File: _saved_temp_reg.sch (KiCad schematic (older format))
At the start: 133 parts, among them IC1 ATMEGA644-P, P1 CONN_01X02, P10 CONN_01X04, P11 CONN_01X06, P12 CONN_01X02, P13 CONN_01X02, P15 CONN_01X02, P2 CONN_01X03, P3 CONN_01X03, P4 CONN_2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

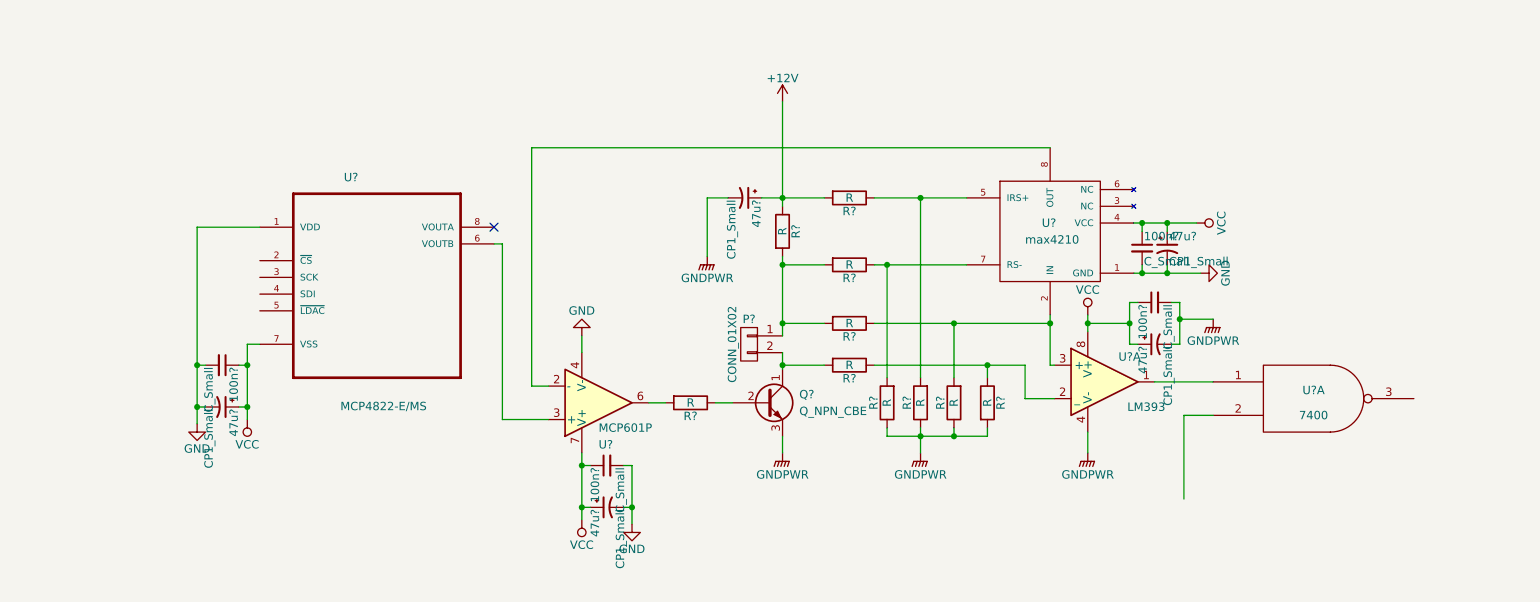
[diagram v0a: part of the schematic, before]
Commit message: change to power opamp
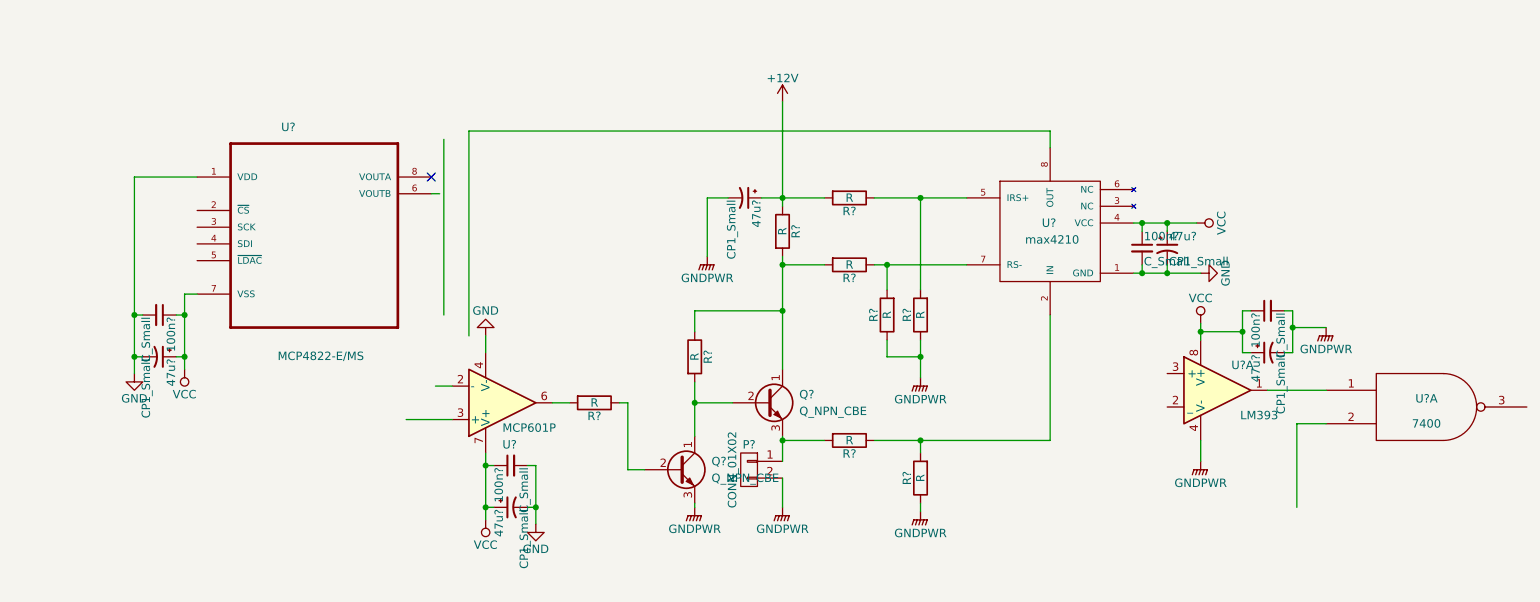
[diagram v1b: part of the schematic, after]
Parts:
- removed P?: CONN_01X02, symbol CONN_01X02
- removed R? (x2): R, symbol R
- added P?: CONN_01X02, symbol CONN_01X02
- added Q?: Q_NPN_CBE, symbol Q_NPN_CBE
- added R?: R, symbol R
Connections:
- net GNDPWR: now also P?.2 (P2), Q?.3 (E); no longer Q?.3 (E)
- net at Q?.1 (C): now also R?.2, R?.2, R?.1
- net at R?.1, R?.2, U?.2 (IN): no longer U?.3 (+)
- net at U?.8 (OUT): no longer U?.2 (-)
- net at Q?.2 (B): now also Q?.1 (C), R?.2; no longer R?.1
- net at U?.3 (+): no longer U?.6 (VOUTB)
- new net: P?.1 (P1), Q?.3 (E), R?.2
- new net: Q?.2 (B), R?.1
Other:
- moved on the sheet: 100n?, 47u?, R?, U?, U?A
